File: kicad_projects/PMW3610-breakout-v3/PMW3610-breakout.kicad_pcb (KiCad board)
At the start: 2 copper layers, 17.6 x 16.6 mm, 18 parts, among them J1 Conn_01x06_Pin, J2 Conn_01x01_Pin, J3 Conn_01x01_Pin, J4 Conn_01x01_Pin, J5 Conn_01x01_Pin, J6 Conn_01x01_Pin, J7 Conn_01x01_Pin, U1 PMW3610, U2 TLV70018_SOT23-5

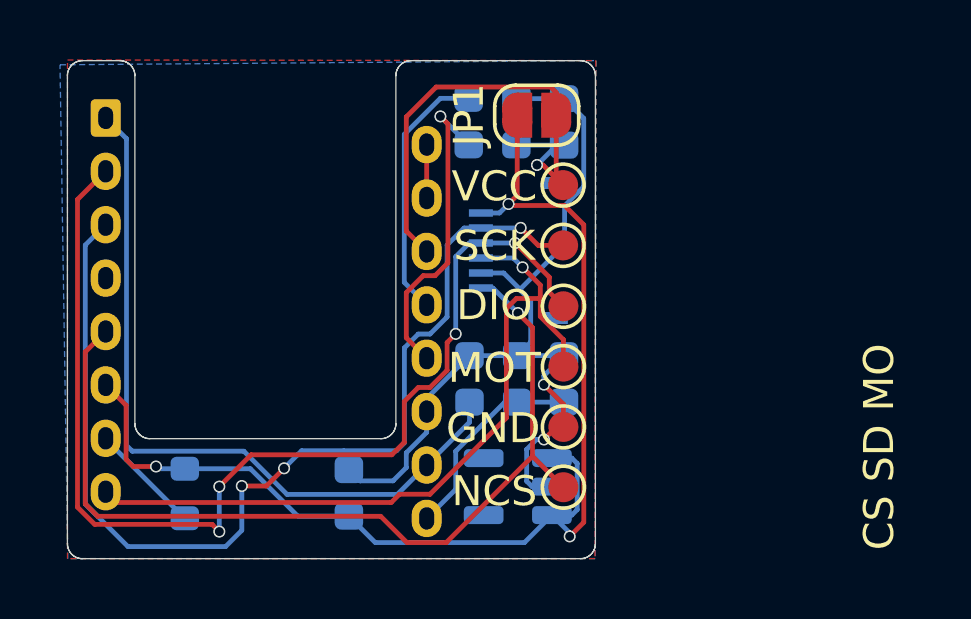
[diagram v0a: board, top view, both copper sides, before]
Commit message: Fix missing wire in V3
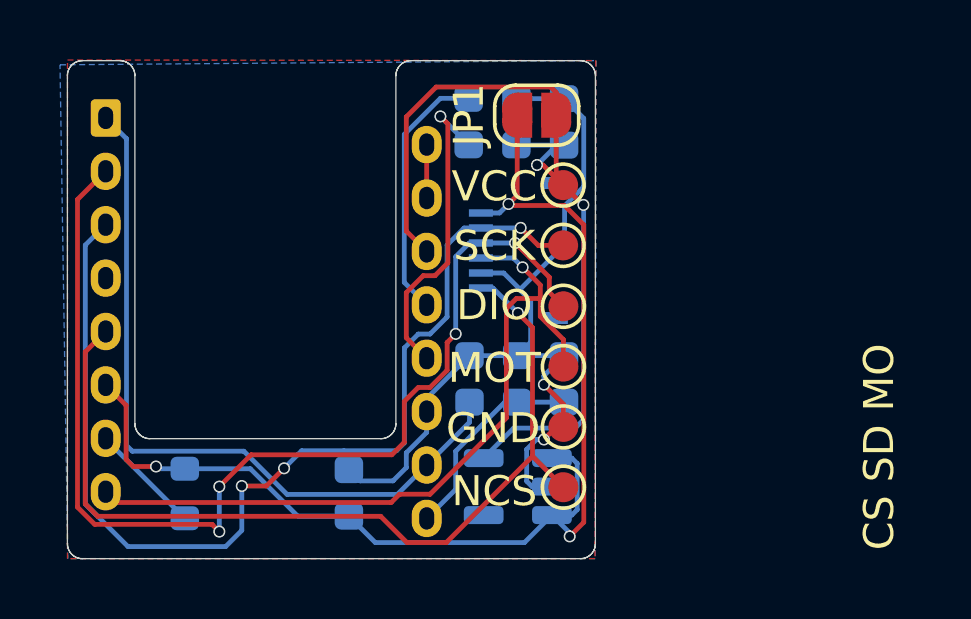
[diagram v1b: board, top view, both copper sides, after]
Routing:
- net VCC_1.8V: track 17.8 -> 29.7 mm, vias 1 -> 2
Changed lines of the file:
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@@
 		)
 		(property "Value" "100nF"
-			(at 2.8 -0.17 360)
+			(at 2.8 -0.17 0)
 			(layer "F.Fab")
 			(effects
@@
 		)
 		(fp_text user "${REFERENCE}"
-			(at 0 0 360)
+			(at 0 0 0)
 			(layer "B.Fab")
 			(effects
@@
 	)
 	(segment
+		(start 42.17657 32.32)
+		(end 42.16 32.32)
+		(width 0.16)
+		(layer "F.Cu")
+		(net 2)
+	)
+	(segment
 		(start 37.27 28.39)
 		(end 36.2732 29.3868)
@@
 		(width 0.16)
 		(layer "F.Cu")
+		(net 2)
+	)
+	(segment
+		(start 42.16 32.32)
+		(end 41.5 31.66)
+		(width 0.16)
+		(layer "F.Cu")
+		(net 2)
+	)
+	(via
+		(at 42.17657 32.32)
+		(size 0.4)
+		(drill 0.3)
+		(layers "F.Cu" "B.Cu")
 		(net 2)
 	)
@@
 	)
 	(segment
+		(start 42.185 32.32843)
+		(end 42.17657 32.32)
+		(width 0.16)
+		(layer "B.Cu")
+		(net 2)
+	)
+	(segment
 		(start 41.5332 30.3283)
 		(end 41.2917 30.3283)
@@
 	)
 	(segment
+		(start 41.9 39.76)
+		(end 42.185 39.475)
+		(width 0.16)
+		(layer "B.Cu")
+		(net 2)
+	)
+	(segment
+		(start 38.8525 40.76)
+		(end 39.8525 39.76)
+		(width 0.16)
+		(layer "B.Cu")
+		(net 2)
+	)
+	(segment
+		(start 42.185 39.475)
+		(end 42.185 32.32843)
+		(width 0.16)
+		(layer "B.Cu")
+		(net 2)
+	)
+	(segment
 		(start 39.9532 30.3283)
 		(end 39.9432 30.3183)
@@
 		(width 0.16)
 		(layer "B.Cu")
+		(net 2)
+	)
+	(segment
+		(start 39.8525 39.76)
+		(end 41.9 39.76)
+		(width 0.16)
+		(layer "B.Cu")
